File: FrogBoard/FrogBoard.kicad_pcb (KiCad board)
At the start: 2 copper layers, 59.3 x 50.6 mm, 61 parts, among them J1 Conn_01x10, J10 Conn_01x01, J11 Conn_01x01, J12 Conn_01x02, J13 Conn_01x01, J14 Conn_01x01, J15 Conn_01x01, J16 Conn_01x01, J17 Conn_01x01, J18 Conn_01x01, J19 Conn_01x01, J2 Conn_01x04, J20 Conn_01x01, J21 Conn_01x01, J22 Conn_01x01, J23 Conn_01x01, J24 Conn_01x01, J25 Conn_01x01, J27 Conn_01x01, J28 Conn_01x01, J3 USB_C_Receptacle_USB2.0_16P, J30 Conn_01x02, J4 Stickbox, J5 Conn_01x03_Socket, J6 Conn_01x02, J7 Conn_01x02, J8 Conn_01x01, J9 Conn_01x01, U1 STM32L432KBUx, U2 USBLC6-2P6, U3 MCP1700T-3302E, U4 BL1555

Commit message: Update footprint and put back micro USB
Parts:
- removed J3: USB_C_Receptacle_USB2.0_16P, FrogBoard_footprints:CONN16_C16PIN_SHN
- removed R10, R8: 5.1k, Resistor_SMD:R_0603_1608Metric_Pad0.98x0.95mm_HandSolder
- added J26: USB_B_Micro, FrogBoard_footprints:AMPHENOL_10118194-0001LF, F.Cu at (-33.5, 4.20)
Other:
- outline, holes or cut-outs redrawn

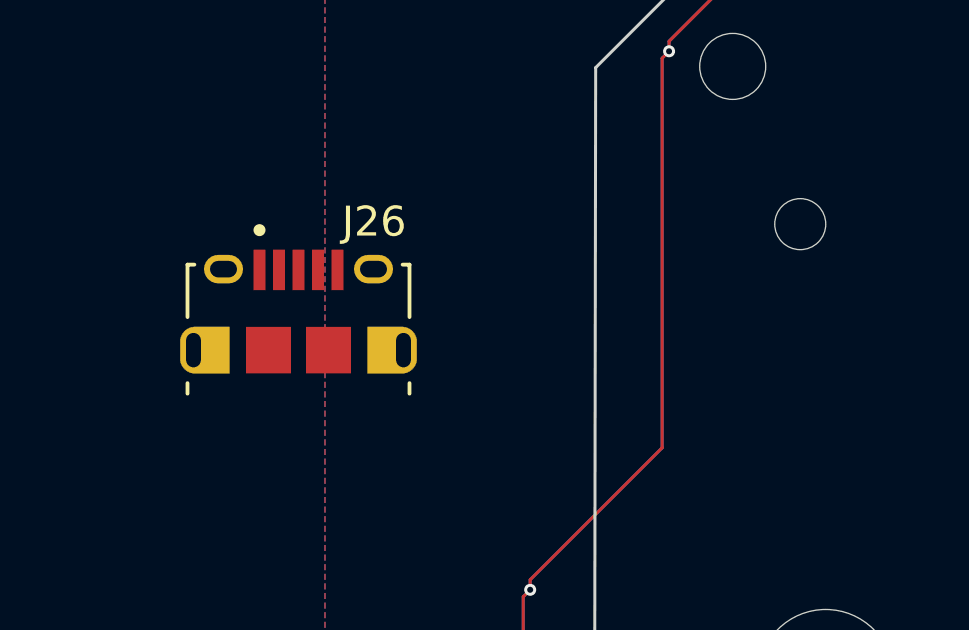
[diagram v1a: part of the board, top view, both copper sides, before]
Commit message: move usb into correct position
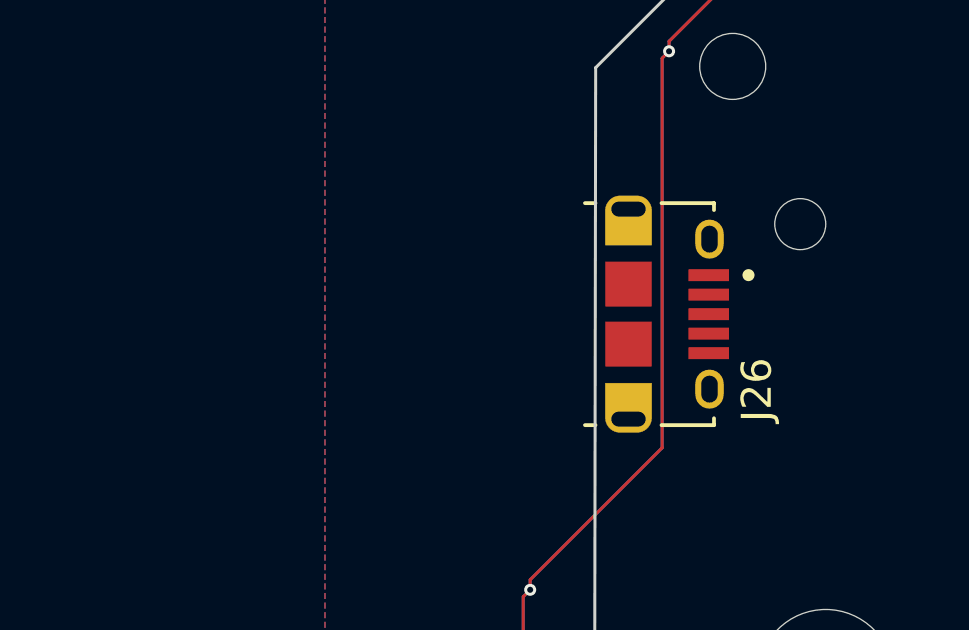
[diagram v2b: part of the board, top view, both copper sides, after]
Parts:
- moved J26 11.1 mm to (-22.5, 3.00), turned to -90 degrees
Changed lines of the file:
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@@
 	(footprint "FrogBoard_footprints:AMPHENOL_10118194-0001LF"
 		(layer "F.Cu")
-		(at -33.5 4.2)
+		(at -22.5 3 -90)
 		(property "Reference" "J26"
-			(at 2.521861 -4.27921 0)
+			(at 2.521861 -4.27921 90)
 			(layer "F.SilkS")
 			(effects
@@
 		)
 		(property "Value" "USB_B_Micro"
-			(at 11.24 -4.635 0)
+			(at 11.24 -4.635 90)
 			(layer "F.Fab")
 			(effects
@@
 		)
 		(property "Datasheet" "https://www.lcsc.com/datasheet/C132563.pdf"
-			(at 0 0 0)
+			(at 0 0 90)
 			(layer "F.Fab")
 			(hide yes)
@@
 		)
 		(property "Description" "USB Micro Type B connector"
-			(at 0 0 0)
+			(at 0 0 90)
 			(layer "F.Fab")
 			(hide yes)
@@
 		)
 		(property "LCSC" "C132563"
-			(at 0 0 0)
+			(at 0 0 270)
 			(unlocked yes)
 			(layer "F.Fab")
@@
 		)
 		(property "MPN" "10118194-0001LF"
-			(at 0 0 0)
+			(at 0 0 270)
 			(unlocked yes)
 			(layer "F.Fab")
@@
 		)
 		(fp_line
+			(start -3.7 1.45)
+			(end -3.7 1.1)
+			(stroke
+				(width 0.127)
+				(type solid)
+			)
+			(layer "F.SilkS")
+		)
+		(fp_line
+			(start 3.7 1.1)
+			(end 3.7 1.45)
+			(stroke
+				(width 0.127)
+				(type solid)
+			)
+			(layer "F.SilkS")
+		)
+		(fp_line
+			(start -3.7 -1.1)
+			(end -3.7 -2.85)
+			(stroke
+				(width 0.127)
+				(type solid)
+			)
+			(layer "F.SilkS")
+		)
+		(fp_line
 			(start -3.7 -2.85)
 			(end -3.47 -2.85)
@@
 		)
 		(fp_line
-			(start -3.7 -1.1)
-			(end -3.7 -2.85)
-			(stroke
-				(width 0.127)
-				(type solid)
-			)
-			(layer "F.SilkS")
-		)
-		(fp_line
-			(start -3.7 1.45)
-			(end -3.7 1.1)
-			(stroke
-				(width 0.127)
-				(type solid)
-			)
-			(layer "F.SilkS")
-		)
-		(fp_line
 			(start 3.47 -2.85)
 			(end 3.7 -2.85)
@@
 			(start 3.7 -2.85)
 			(end 3.7 -1.1)
-			(stroke
-				(width 0.127)
-				(type solid)
-			)
-			(layer "F.SilkS")
-		)
-		(fp_line
-			(start 3.7 1.1)
-			(end 3.7 1.45)
 			(stroke
 				(width 0.127)
@@
 		)
 		(fp_line
+			(start -4.275 2.93)
+			(end 4.275 2.93)
+			(stroke
+				(width 0.05)
+				(type solid)
+			)
+			(layer "F.CrtYd")
+		)
+		(fp_line
+			(start 4.275 2.93)
+			(end 4.275 -3.6)
+			(stroke
+				(width 0.05)
+				(type solid)
+			)
+			(layer "F.CrtYd")
+		)
+		(fp_line
 			(start -4.275 -3.6)
 			(end -4.275 2.93)
@@
 		)
 		(fp_line
-			(start -4.275 2.93)
-			(end 4.275 2.93)
-			(stroke
-				(width 0.05)
-				(type solid)
-			)
-			(layer "F.CrtYd")
-		)
-		(fp_line
 			(start 4.275 -3.6)
 			(end -4.275 -3.6)
@@
 		)
 		(fp_line
-			(start 4.275 2.93)
-			(end 4.275 -3.6)
-			(stroke
-				(width 0.05)
-				(type solid)
-			)
-			(layer "F.CrtYd")
+			(start -4.025 2.68)
+			(end -4.025 2.15)
+			(stroke
+				(width 0.127)
+				(type solid)
+			)
+			(layer "F.Fab")
+		)
+		(fp_line
+			(start 4.025 2.68)
+			(end -4.025 2.68)
+			(stroke
+				(width 0.127)
+				(type solid)
+			)
+			(layer "F.Fab")
+		)
+		(fp_line
+			(start 4.025 2.68)
+			(end 4.025 2.15)
+			(stroke
+				(width 0.127)
+				(type solid)
+			)
+			(layer "F.Fab")
 		)
 		(fp_line
@@
 		)
 		(fp_line
-			(start -4.025 2.68)
-			(end -4.025 2.15)
+			(start -3.7 2.15)
+			(end -3.7 1.45)
+			(stroke
+				(width 0.127)
+				(type solid)
+			)
+			(layer "F.Fab")
+		)
+		(fp_line
+			(start 4.025 2.15)
+			(end 3.7 2.15)
+			(stroke
+				(width 0.127)
+				(type solid)
+			)
+			(layer "F.Fab")
+		)
+		(fp_line
+			(start -3.7 1.45)
+			(end 6.5 1.45)
+			(stroke
+				(width 0.127)
+				(type solid)
+			)
+			(layer "F.Fab")
+		)
+		(fp_line
+			(start -3.7 1.45)
+			(end -3.7 -2.85)
 			(stroke
 				(width 0.127)
@@
 		)
 		(fp_line
-			(start -3.7 1.45)
-			(end -3.7 -2.85)
-			(stroke
-				(width 0.127)
-				(type solid)
-			)
-			(layer "F.Fab")
-		)
-		(fp_line
-			(start -3.7 1.45)
-			(end 6.5 1.45)
-			(stroke
-				(width 0.127)
-				(type solid)
-			)
-			(layer "F.Fab")
-		)
-		(fp_line
-			(start -3.7 2.15)
-			(end -3.7 1.45)
-			(stroke
-				(width 0.127)
-				(type solid)
-			)
-			(layer "F.Fab")
-		)
-		(fp_line
 			(start 3.7 -2.85)
 			(end 3.7 2.15)
-			(stroke
-				(width 0.127)
-				(type solid)
-			)
-			(layer "F.Fab")
-		)
-		(fp_line
-			(start 4.025 2.15)
-			(end 3.7 2.15)
-			(stroke
-				(width 0.127)
-				(type solid)
-			)
-			(layer "F.Fab")
-		)
-		(fp_line
-			(start 4.025 2.68)
-			(end -4.025 2.68)
-			(stroke
-				(width 0.127)
-				(type solid)
-			)
-			(layer "F.Fab")
-		)
-		(fp_line
-			(start 4.025 2.68)
-			(end 4.025 2.15)
 			(stroke
 				(width 0.127)
@@
 		)
 		(fp_text user "PCB EDGE"
-			(at 4.25 1.25 0)
+			(at 4.25 1.25 90)
 			(layer "F.Fab")
 			(effects
@@
 		)
 		(pad "1" smd rect
-			(at -1.3 -2.675)
+			(at -1.3 -2.675 270)
 			(size 0.4 1.35)
 			(layers "F.Cu" "F.Mask" "F.Paste")
@@
 		)
 		(pad "2" smd rect
-			(at -0.65 -2.675)
+			(at -0.65 -2.675 270)
 			(size 0.4 1.35)
 			(layers "F.Cu" "F.Mask" "F.Paste")
@@
 		)
 		(pad "3" smd rect
-			(at 0 -2.675)
+			(at 0 -2.675 270)
 			(size 0.4 1.35)
 			(layers "F.Cu" "F.Mask" "F.Paste")
@@
 		)
 		(pad "4" smd rect
-			(at 0.65 -2.675)
+			(at 0.65 -2.675 270)
 			(size 0.4 1.35)
 			(layers "F.Cu" "F.Mask" "F.Paste")
@@
 		)
 		(pad "5" smd rect
-			(at 1.3 -2.675)
+			(at 1.3 -2.675 270)
 			(size 0.4 1.35)
 			(layers "F.Cu" "F.Mask" "F.Paste")
@@
 		)
 		(pad "6" thru_hole custom
-			(at -3.5 0)
+			(at -3.5 0 270)
 			(size 0.775 0.775)
 			(drill oval 0.5 1.15)
@@
 		)
 		(pad "6" thru_hole oval
-			(at -2.5 -2.7)
+			(at -2.5 -2.7 270)
 			(size 1.3 0.95)
 			(drill oval 0.9 0.55)
@@
 		)
 		(pad "6" smd rect
-			(at -1 0)
+			(at -1 0 270)
 			(size 1.5 1.55)
 			(layers "F.Cu" "F.Mask" "F.Paste")
@@
 		)
 		(pad "6" smd rect
-			(at 1 0)
+			(at 1 0 270)
 			(size 1.5 1.55)
 			(layers "F.Cu" "F.Mask" "F.Paste")
@@
 		)
 		(pad "6" thru_hole oval
-			(at 2.5 -2.7)
+			(at 2.5 -2.7 270)
 			(size 1.3 0.95)
 			(drill oval 0.9 0.55)
@@
 		)
 		(pad "6" thru_hole custom
-			(at 3.5 0)
+			(at 3.5 0 270)
 			(size 0.775 0.775)
 			(drill oval 0.5 1.15)

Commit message: bulk rounting done
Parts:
- added J29: Conn_01x01, FrogBoard_footprints:FrogBoard_PinHeader_1x01_P1.00mm_Vertical, F.Cu at (-19.1, 8.84)
- added J3: Conn_01x01, FrogBoard_footprints:FrogBoard_PinHeader_1x01_P1.00mm_Vertical, F.Cu at (-23.6, 26.9)
- added J31: Conn_01x01, FrogBoard_footprints:FrogBoard_PinHeader_1x01_P1.00mm_Vertical, F.Cu at (-20.3, 8.28)
- added J32: Conn_01x01, FrogBoard_footprints:FrogBoard_PinHeader_1x01_P1.00mm_Vertical, F.Cu at (-18.0, 8.28)
- added J33: Conn_01x01, FrogBoard_footprints:FrogBoard_PinHeader_1x01_P1.00mm_Vertical, F.Cu at (-21.5, 8.84)
- J12: value Conn_01x02 -> Conn_01x01; footprint FrogBoard_footprints:PinHeader_1x02_P1.00mm_Vertical_Neutral_No_Coutryard -> FrogBoard_footprints:FrogBoard_PinHeader_1x01_P1.00mm_Vertical
- moved C1 67.8 mm to (-11.2, -10.8), turned to 180 degrees
- moved C4 52.0 mm to (-11.8, 23.9), turned to 180 degrees
- moved F1 46.7 mm to (-27.1, 27.8), turned to -90 degrees
- moved J6 46.5 mm to (-8.01, 24.7), turned to 180 degrees
- moved U1 42.5 mm to (-16.9, 23.9), turned to 180 degrees
- moved C8 40.6 mm to (-9.40, 24.5), turned to -90 degrees
- moved J9 38.6 mm to (-11.9, 22.0)
- moved J14 35.8 mm to (-23.2, 25.7)
- moved C6 35.8 mm to (-24.8, 31.2), turned to 45 degrees
- moved D3 35.6 mm to (-8.84, 19.3), turned to -90 degrees
- moved R7 33.9 mm to (-10.4, 19.3), turned to 90 degrees
- moved C11 33.2 mm to (-14.2, 33.1)
- moved J12 31.6 mm to (-23.1, 28.1), turned to 0 degrees
- moved J10 31.2 mm to (-8.51, 21.9)
- moved J11 30.0 mm to (-10.6, 25.8)
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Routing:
- net GND: track 1208.4 -> 1787.2 mm, vias 116 -> 246
- net +3.3V: track 71.2 -> 211.7 mm, vias 2 -> 7
- net AY_IN: track 0.00 -> 72.1 mm
- net STICK_BTN: track 0.00 -> 55.2 mm, vias 0 -> 1
- net AX_IN: track 0.00 -> 51.4 mm
- net VBUS: track 0.00 -> 35.5 mm
- net /USB_RAW-: track 0.00 -> 19.4 mm
- net /USB_RAW+: track 0.00 -> 17.8 mm
- net BOOT_SEL: track 0.00 -> 14.1 mm
- net FFC_P2: track 46.1 -> 60.0 mm, vias 0 -> 1
- net SDA: track 76.8 -> 90.5 mm, vias 0 -> 1
- net USB+: track 0.00 -> 13.2 mm
- net FFC_P4: track 52.7 -> 65.6 mm, vias 0 -> 1
- net A_SEL: track 48.9 -> 60.6 mm, vias 0 -> 1
- net USB-: track 0.00 -> 11.0 mm
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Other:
- outline, holes or cut-outs redrawn

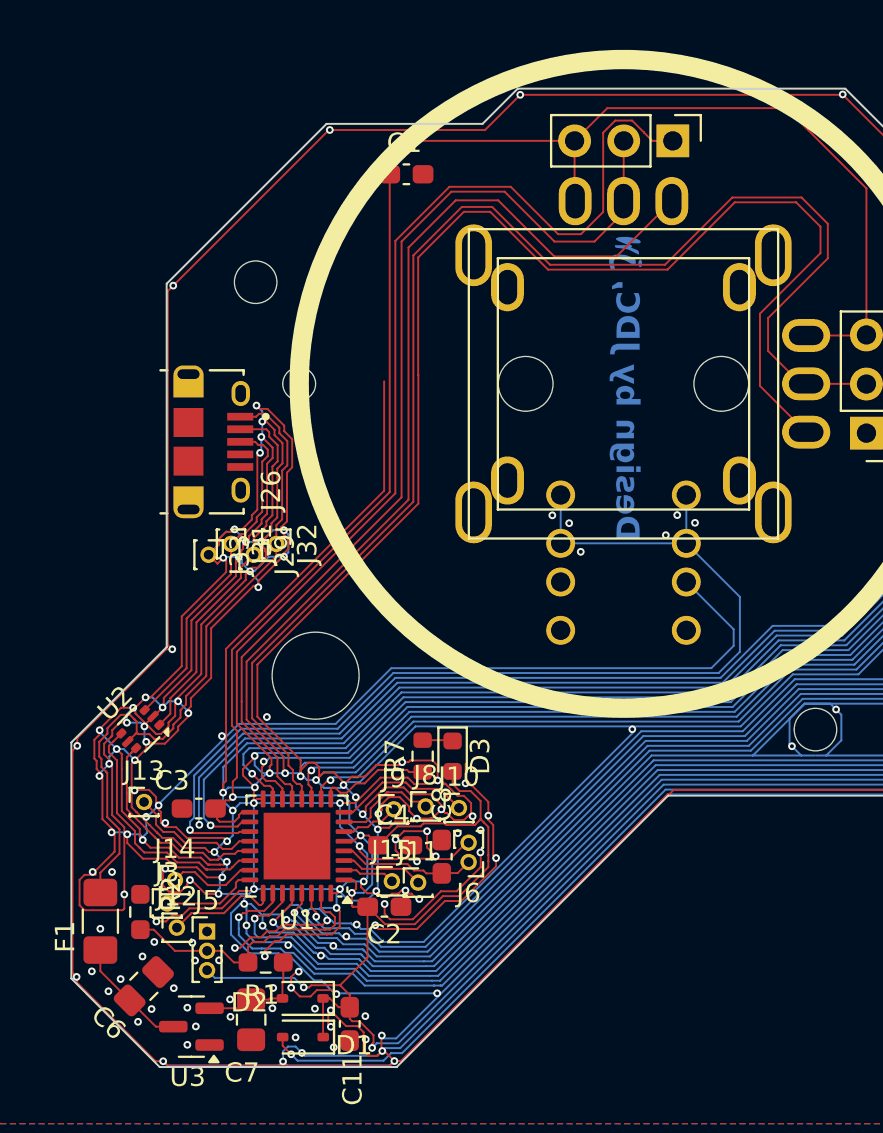
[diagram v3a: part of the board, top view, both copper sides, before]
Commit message: moved MCU south a bit for better routing
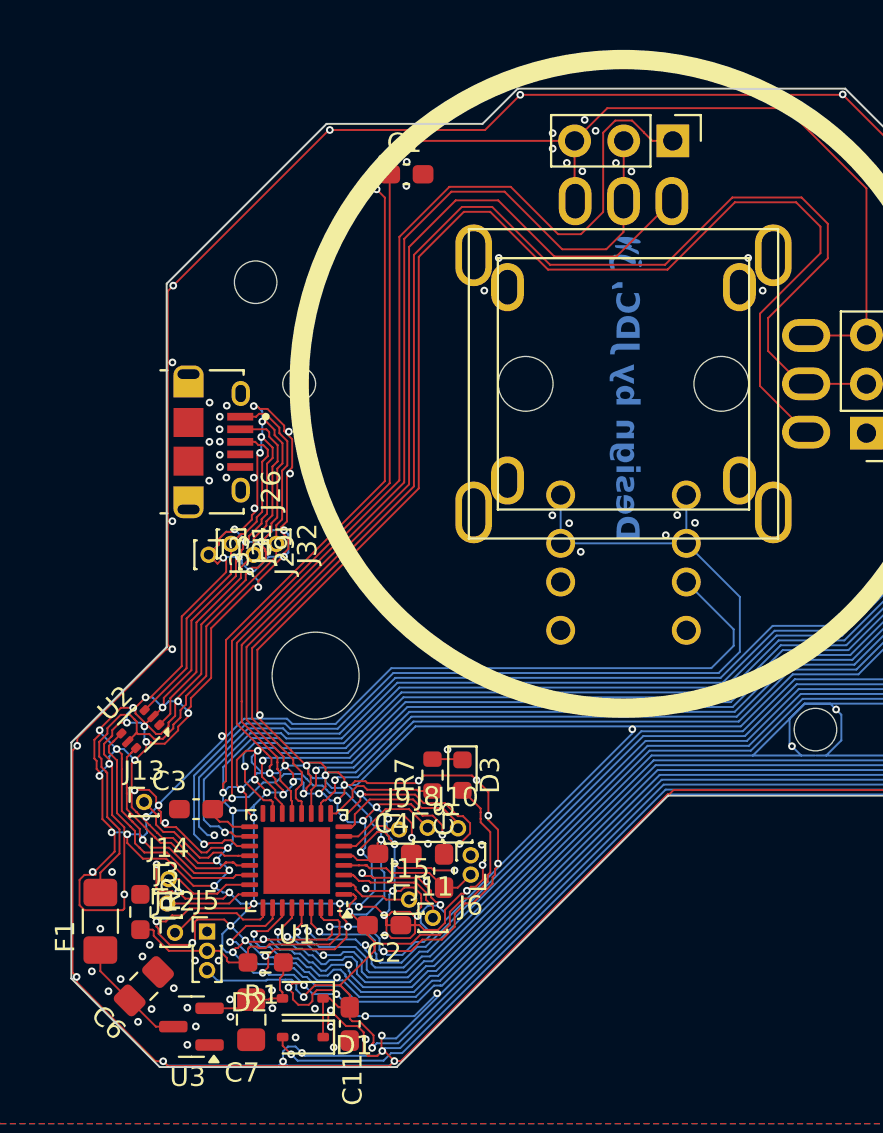
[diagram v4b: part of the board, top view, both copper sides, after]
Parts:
- moved J11 1.97 mm to (-9.86, 27.6)
- moved J15 1.30 mm to (-11.1, 26.7)
- moved R7 1.10 mm to (-9.88, 20.2)
- moved D3 1.10 mm to (-8.33, 20.2)
- moved J8 1.10 mm to (-10.1, 23.0)
- moved J9 1.07 mm to (-11.6, 23.1)
- moved J10 1.05 mm to (-8.56, 23.0)
- moved C2 0.95 mm to (-12.4, 28.0)
- moved U1 0.75 mm to (-16.9, 24.7)
- moved C8 0.75 mm to (-9.28, 25.2)
- moved J6 0.66 mm to (-7.90, 25.4)
- moved C4 0.44 mm to (-11.8, 24.3)
- moved J14 0.33 mm to (-23.5, 25.6)
- moved J12 0.28 mm to (-23.2, 28.4)
- moved C3 0.14 mm to (-22.1, 22.0)
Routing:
- net GND: track 1787.2 -> 1821.8 mm, vias 246 -> 289
- net +3.3V: track 211.7 -> 208.9 mm
- net Unused_10: track 4.30 -> 6.08 mm
- net AX_IN: track 51.4 -> 53.0 mm
- net Unused_9: track 2.71 -> 3.76 mm
- net FFC_P5: track 55.9 -> 56.9 mm
- net AY_IN: track 72.1 -> 73.1 mm
- net FFC_P3: track 56.7 -> 57.5 mm
- net FFC_P4: track 65.6 -> 66.4 mm
- net SCL: track 85.7 -> 86.4 mm
- net SDA: track 90.5 -> 91.1 mm
- net AX_OUT: track 44.8 -> 45.4 mm
- net FFC_P6: track 57.4 -> 58.0 mm

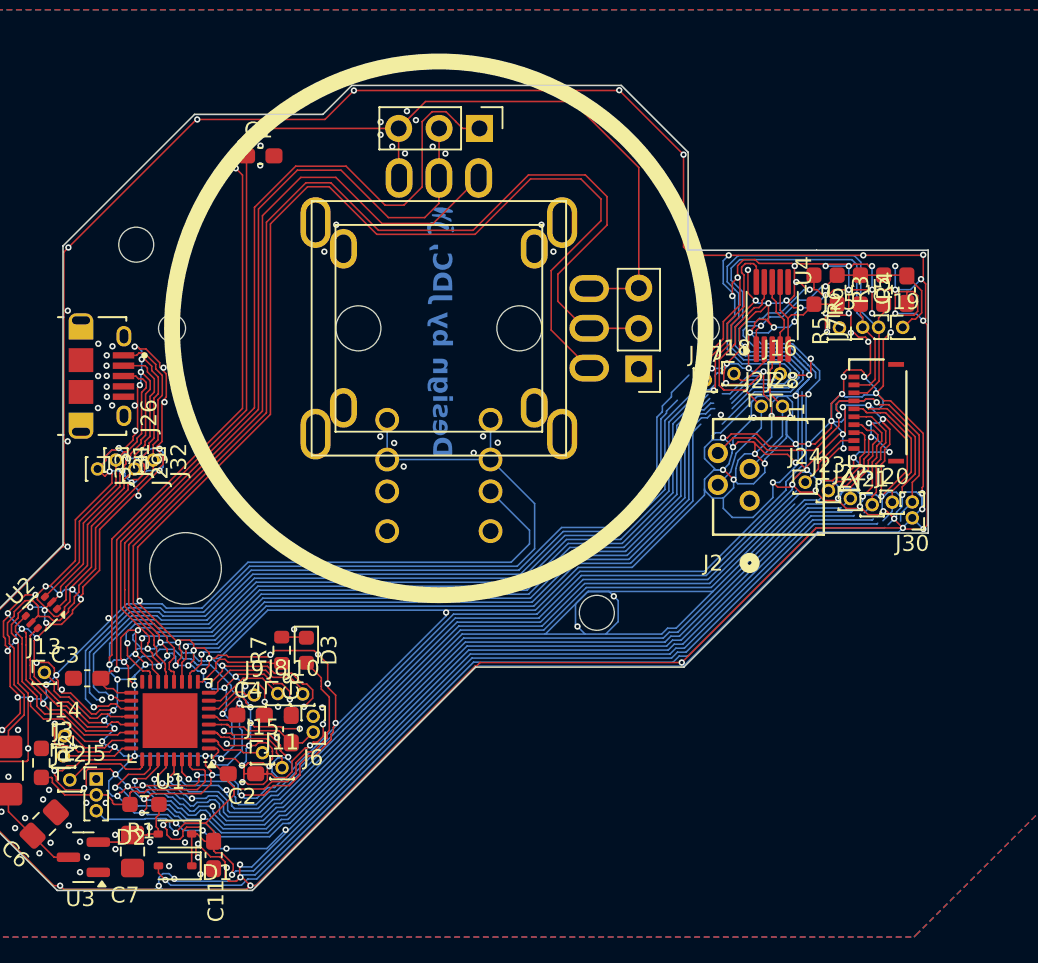
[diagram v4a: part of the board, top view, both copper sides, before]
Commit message: electrically correct
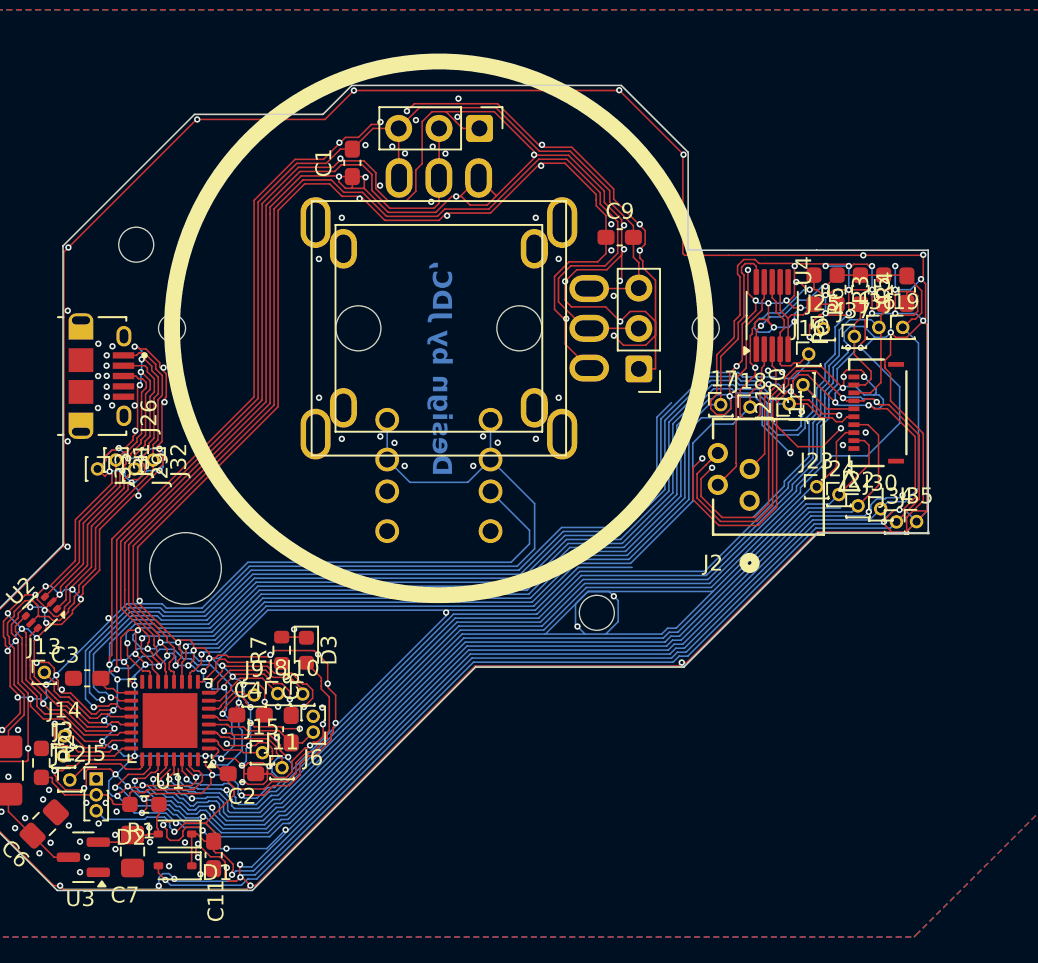
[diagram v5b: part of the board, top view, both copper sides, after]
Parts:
- removed J27, J28: Conn_01x01, FrogBoard_footprints:FrogBoard_PinHeader_1x01_P1.00mm_Vertical
- removed J7: Conn_01x02, FrogBoard_footprints:PinHeader_1x02_P1.00mm_Vertical_Neutral_No_Coutryard
- added C9: 100nF, Capacitor_SMD:C_0603_1608Metric_Pad1.08x0.95mm_HandSolder, F.Cu at (11.4, -5.72)
- added J34: Conn_01x01, FrogBoard_footprints:FrogBoard_PinHeader_1x01_P1.00mm_Vertical, F.Cu at (28.8, 12.2)
- added J35: Conn_01x01, FrogBoard_footprints:FrogBoard_PinHeader_1x01_P1.00mm_Vertical, F.Cu at (30.0, 12.2)
- added J36: Conn_01x01, FrogBoard_footprints:FrogBoard_PinHeader_1x01_P1.00mm_Vertical, F.Cu at (27.7, -0.06)
- added J37: Conn_01x01, FrogBoard_footprints:FrogBoard_PinHeader_1x01_P1.00mm_Vertical, F.Cu at (26.1, 0.51)
- J30: value Conn_01x02 -> Conn_01x01; footprint FrogBoard_footprints:PinHeader_1x02_P1.00mm_Vertical_Neutral_No_Coutryard -> FrogBoard_footprints:FrogBoard_PinHeader_1x01_P1.00mm_Vertical
- moved J20 9.27 mm to (22.9, 3.55), turned to 90 degrees
- moved J21 8.21 mm to (22.0, 4.75), turned to 90 degrees
- moved C1 5.81 mm to (-5.44, -10.4), turned to 90 degrees
- moved J18 2.33 mm to (19.6, 4.95)
- moved J24 2.26 mm to (25.1, 10.4)
- moved J16 2.18 mm to (23.2, 1.62)
- moved J30 2.06 mm to (27.8, 11.3), turned to 0 degrees
- moved J17 1.83 mm to (17.7, 4.80)
- moved J25 1.01 mm to (24.2, 0.02)
- moved J23 0.78 mm to (23.8, 9.96)
- moved J22 0.66 mm to (26.4, 11.2)
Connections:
- J30 pad 1: GND -> +3.3V
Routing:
- net SDA: track 91.1 -> 69.8 mm
- net SCL: track 86.4 -> 68.2 mm
- net GND: track 1821.8 -> 1834.9 mm, vias 289 -> 279
- net +3.3V_HORI: track 81.9 -> 92.7 mm
- net A_SEL: track 61.0 -> 68.7 mm
- net FFC_P6: track 58.0 -> 63.1 mm
- net AX_OUT: track 45.4 -> 49.2 mm
- net FFC_P5: track 56.9 -> 60.2 mm
- net AY_MUX_OUT: track 17.0 -> 14.0 mm
- net AY_IN: track 73.1 -> 75.2 mm
- net +3.3V: track 208.9 -> 210.7 mm
- net AY_OUT: track 54.5 -> 56.2 mm
- net FFC_P2: track 60.4 -> 62.0 mm
- net STICK_BTN: track 55.7 -> 56.9 mm
- net FFC_P3: track 57.5 -> 58.6 mm
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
